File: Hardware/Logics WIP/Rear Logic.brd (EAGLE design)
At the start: 123.8 x 41.3 mm, 207 parts

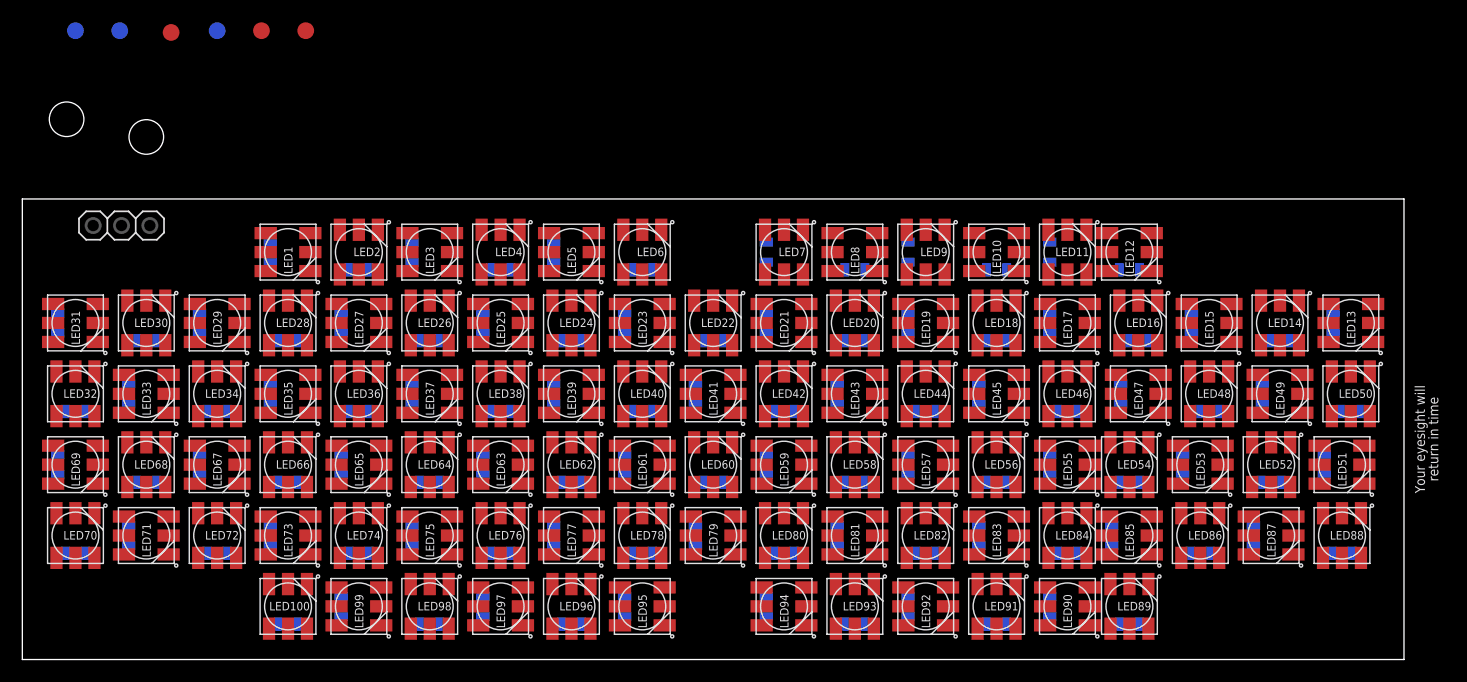
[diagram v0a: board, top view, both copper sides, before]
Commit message: 
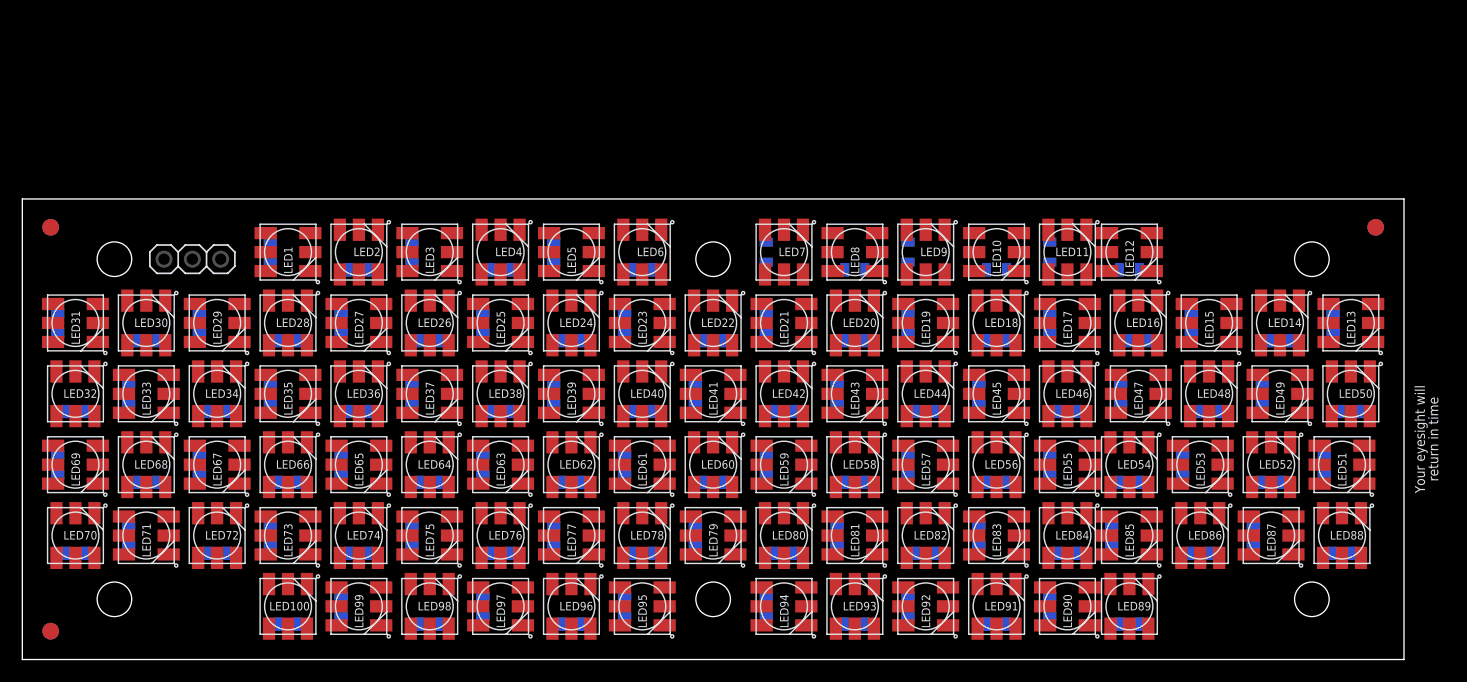
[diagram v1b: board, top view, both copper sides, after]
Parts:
- moved FID5 105.3 mm to (121.3, 38.7)
- moved FID1 97.5 mm to (121.3, 38.7)
- moved FID2 54.7 mm to (2.54, 2.54)
- moved FID4 53.9 mm to (2.54, 2.54)
- moved FID3 25.8 mm to (2.54, 38.7)
- moved FID6 18.7 mm to (2.54, 38.7)
- moved IN 7.03 mm to (15.2, 35.9)
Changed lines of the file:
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@@
 <setting verticaltext="up"/>
 </settings>
-<grid distance="0.03125" unitdist="inch" unit="inch" style="lines" multiple="1" display="yes" altdistance="0.0625" altunitdist="inch" altunit="inch"/>
+<grid distance="0.01" unitdist="inch" unit="inch" style="lines" multiple="1" display="yes" altdistance="0.0625" altunitdist="inch" altunit="inch"/>
 <layers>
 <layer number="1" name="Top" color="4" fill="1" visible="yes" active="yes"/>
@@
 <board>
 <plain>
-<text x="16.66875" y="44.45" size="1.397" layer="26" font="vector" rot="MR270">+ -</text>
+<text x="23.8125" y="49.2125" size="1.397" layer="26" font="vector" rot="MR270">+ -</text>
 <wire x1="0" y1="0" x2="0" y2="41.275" width="0" layer="20"/>
 <wire x1="0" y1="41.275" x2="123.825" y2="41.275" width="0" layer="20"/>
 <wire x1="123.825" y1="41.275" x2="123.825" y2="0" width="0" layer="20"/>
 <wire x1="123.825" y1="0" x2="0" y2="0" width="0" layer="20"/>
-<hole x="3.96875" y="48.41875" drill="3.1"/>
-<hole x="11.1125" y="46.83125" drill="3.1"/>
+<hole x="61.9125" y="35.8775" drill="3.1"/>
+<hole x="8.255" y="35.8775" drill="3.1"/>
 <text x="125.857" y="19.7485" size="0.889" layer="21" font="vector" distance="35" rot="R90" align="center">Your eyesight will
 return in time</text>
+<hole x="8.255" y="5.3975" drill="3.1"/>
+<hole x="61.9125" y="5.3975" drill="3.1"/>
+<hole x="115.57" y="35.8775" drill="3.1"/>
+<hole x="115.57" y="5.3975" drill="3.1"/>
 </plain>
 <attributes>
@@
 <element name="LED8" library="rseries" package="WS2812" value="WS2812" x="74.6125" y="36.5125"/>
 <element name="C8" library="SparkFun-Capacitors" package="0805" value="0.1uF" x="74.6125" y="34.925" smashed="yes" rot="MR180"/>
-<element name="FID1" library="SparkFun-Aesthetics" package="FIDUCIAL-1.5X3" value="FIDUCIAL1.5X3" x="25.4" y="56.35625"/>
-<element name="FID2" library="SparkFun-Aesthetics" package="FIDUCIAL-1.5X3" value="FIDUCIAL1.5X3" x="13.335" y="56.1975"/>
-<element name="FID3" library="SparkFun-Aesthetics" package="FIDUCIAL-1.5X3" value="FIDUCIAL1.5X3" x="21.43125" y="56.35625"/>
-<element name="FID4" library="SparkFun-Aesthetics" package="FIDUCIAL-1.5X3" value="FIDUCIAL1.5X3" x="4.7625" y="56.35625" rot="MR0"/>
-<element name="FID5" library="SparkFun-Aesthetics" package="FIDUCIAL-1.5X3" value="FIDUCIAL1.5X3" x="17.4625" y="56.35625" rot="MR0"/>
-<element name="FID6" library="SparkFun-Aesthetics" package="FIDUCIAL-1.5X3" value="FIDUCIAL1.5X3" x="8.73125" y="56.35625" rot="MR0"/>
-<element name="IN" library="adafruit" package="1X03" value="" x="8.89" y="38.89375" smashed="yes" rot="R180">
-<attribute name="NAME" x="7.2517" y="40.4622" size="1.143" layer="26" font="vector" ratio="10" rot="MR0"/>
-<attribute name="VALUE" x="12.7" y="42.06875" size="1.27" layer="27" rot="R180"/>
+<element name="FID1" library="SparkFun-Aesthetics" package="FIDUCIAL-1.5X3" value="FIDUCIAL1.5X3" x="121.285" y="38.735"/>
+<element name="FID2" library="SparkFun-Aesthetics" package="FIDUCIAL-1.5X3" value="FIDUCIAL1.5X3" x="2.54" y="2.54"/>
+<element name="FID3" library="SparkFun-Aesthetics" package="FIDUCIAL-1.5X3" value="FIDUCIAL1.5X3" x="2.54" y="38.735"/>
+<element name="FID4" library="SparkFun-Aesthetics" package="FIDUCIAL-1.5X3" value="FIDUCIAL1.5X3" x="2.54" y="2.54" rot="MR0"/>
+<element name="FID5" library="SparkFun-Aesthetics" package="FIDUCIAL-1.5X3" value="FIDUCIAL1.5X3" x="121.285" y="38.735" rot="MR0"/>
+<element name="FID6" library="SparkFun-Aesthetics" package="FIDUCIAL-1.5X3" value="FIDUCIAL1.5X3" x="2.54" y="38.735" rot="MR0"/>
+<element name="IN" library="adafruit" package="1X03" value="" x="15.24" y="35.8775" smashed="yes" rot="R180">
+<attribute name="NAME" x="13.6017" y="37.44595" size="1.143" layer="26" font="vector" ratio="10" rot="MR0"/>
+<attribute name="VALUE" x="19.05" y="39.0525" size="1.27" layer="27" rot="R180"/>
 </element>
 <element name="LED9" library="rseries" package="WS2812" value="WS2812" x="80.9625" y="36.5125" rot="R90"/>
@@
 <wire x1="2.7625" y1="28.4625" x2="5.6625" y2="22.225" width="0" layer="19" extent="1-16"/>
 <wire x1="3.175" y1="29.2625" x2="2.7625" y2="28.4625" width="0" layer="19" extent="1-16"/>
-<wire x1="11.43" y1="38.89375" x2="12.0125" y2="28.575" width="0" layer="19" extent="16-16"/>
+<wire x1="17.78" y1="35.8775" x2="12.0125" y2="28.575" width="0" layer="19" extent="16-16"/>
 </signal>
 <signal name="+5V" class="1">
@@
 <wire x1="3.8625" y1="9.525" x2="3.0625" y2="13.1125" width="0" layer="19" extent="1-16"/>
 <wire x1="4.7625" y1="9.1125" x2="3.8625" y2="9.525" width="0" layer="19" extent="1-16"/>
-<wire x1="8.89" y1="38.89375" x2="9.4125" y2="32.1625" width="0" layer="19" extent="1-1"/>
+<wire x1="15.24" y1="35.8775" x2="9.4125" y2="32.1625" width="0" layer="19" extent="1-1"/>
 </signal>
 <signal name="DIN">
 <contactref element="LED1" pad="DI"/>
 <contactref element="IN" pad="3"/>
-<wire x1="6.35" y1="38.89375" x2="25.8125" y2="36.5125" width="0" layer="19" extent="1-1"/>
+<wire x1="12.7" y1="35.8775" x2="25.8125" y2="36.5125" width="0" layer="19" extent="1-1"/>
 </signal>
 <signal name="N$1">
